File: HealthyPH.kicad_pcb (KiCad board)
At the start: 2 copper layers, 68.4 x 53.2 mm, 33 parts, among them CON1 LB_BarrelJack, P1 CONN_6, P2 V+_WallWart, Q1 TIP122, U1 LMV341, U2 MCP3901, U5 LM7805, X1 CRYSTAL

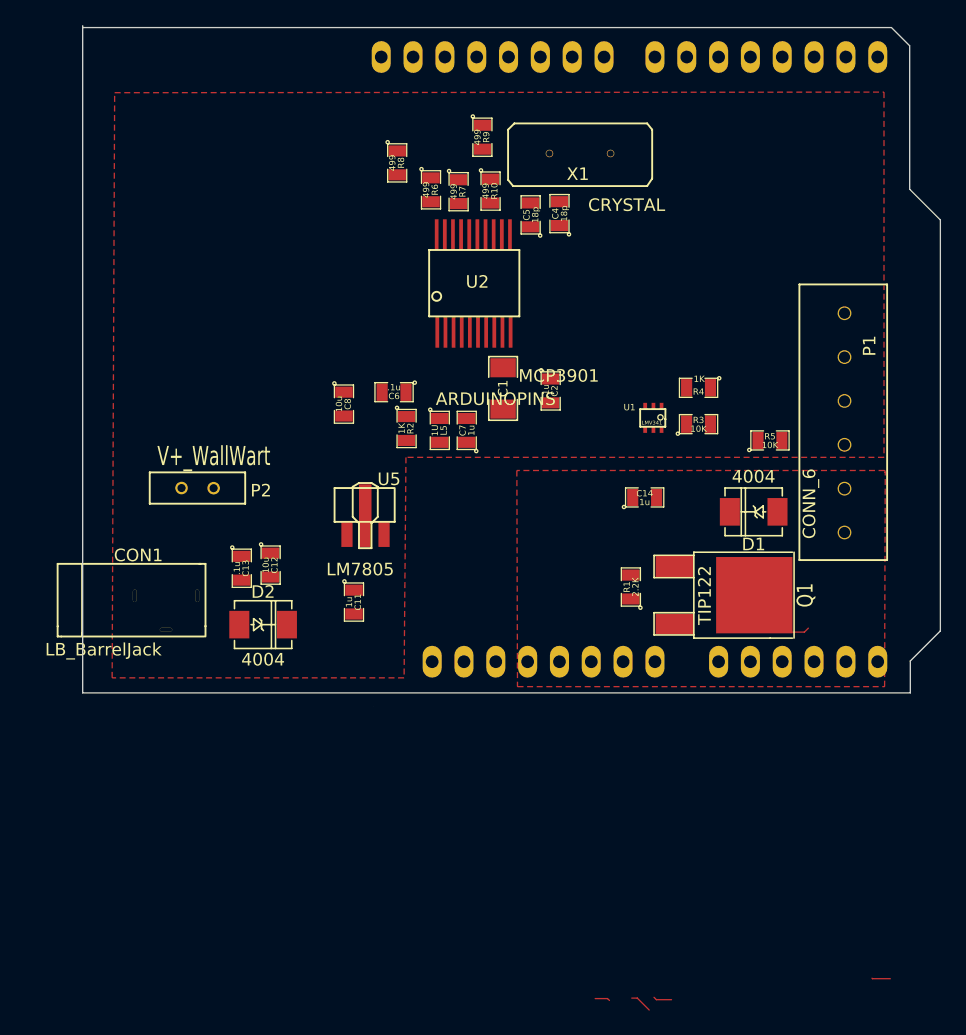
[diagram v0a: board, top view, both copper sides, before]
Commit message: added 2nd pump in circuit to accomodate pH UP
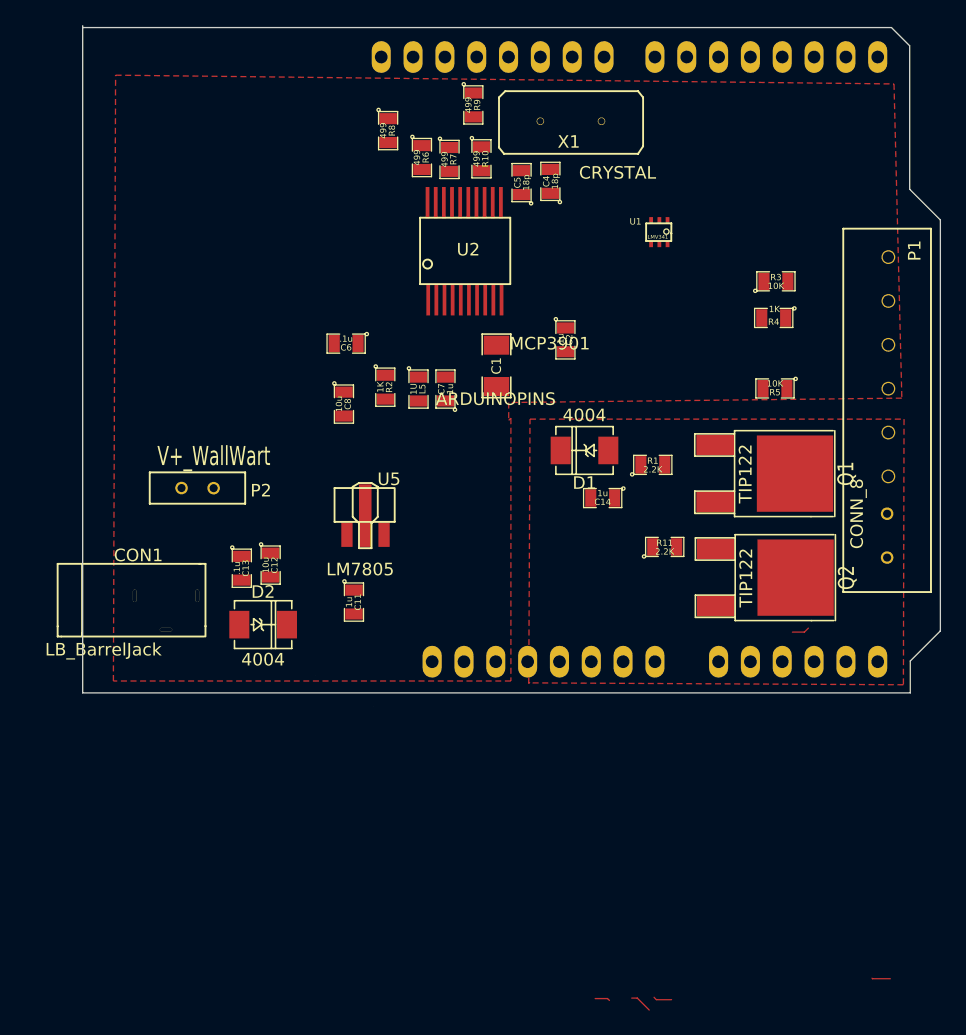
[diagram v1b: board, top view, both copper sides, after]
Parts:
- added Q2: TIP122, DPAK2, F.Cu at (201.6, 109.0)
- added R11: 2.2K, SM0805, F.Cu at (197.4, 106.5)
- P1: value CONN_6 -> CONN_8; footprint LB_6PosTB -> LB_8PosTB
- moved U1 14.8 mm to (198.0, 82.1)
- moved D1 14.4 mm to (191.1, 98.8)
- moved R3 13.0 mm to (206.3, 85.3)
- moved Q1 10.2 mm to (201.5, 100.7)
- moved R1 9.91 mm to (196.5, 100.0), turned to 0 degrees
- moved P1 9.65 mm to (218.7, 81.2)
- moved R4 8.19 mm to (206.2, 88.3)
- moved C6 5.44 mm to (172.0, 90.3)
- moved C2 4.24 mm to (189.5, 90.0)
- moved R5 4.17 mm to (206.2, 93.9), turned to 180 degrees
- moved C7 3.71 mm to (179.9, 94.0)
- moved L5 3.71 mm to (177.8, 94.0)
- moved R2 3.71 mm to (175.2, 93.8)
- moved C14 3.35 mm to (192.5, 102.7), turned to 180 degrees
- moved C4 2.68 mm to (188.3, 77.4)
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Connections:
- net /Arduino/PHPUMPDOWN renamed /Pumps/DownPump
- net /Pumps/Pump_SW renamed /Pumps/SW_DownPump
- ARD1 pad 13: /Arduino/~DR -> (no net)
- ARD1 pad 15: /Arduino/~RESET -> (no net)
- ARD1 pad 21: /Arduino/~CS -> (no net)
- ARD1 pad 22: /Arduino/MOSI -> (no net)
- ARD1 pad 23: /Arduino/MISO -> (no net)
- ARD1 pad 24: /Arduino/SCLK -> (no net)
- ARD1 pad 6: (no net) -> /Arduino/PumpUp
- D1 pad 1: /Pumps/Pump_V+ -> /Pumps/V+_DownPump
- P1 pad 5: /Pumps/Pump_V+ -> /Pumps/V+_DownPump
- R10 pad 1: /Arduino/~DR -> (no net)
- R6 pad 1: /Arduino/SCLK -> (no net)
- R7 pad 1: /Arduino/MISO -> (no net)
- R8 pad 1: /Arduino/MOSI -> (no net)
- R9 pad 1: /Arduino/~CS -> (no net)
- U2 pad 1: /Arduino/~RESET -> (no net)
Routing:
- net /Pumps/SW_DownPump: track 1.40 -> 0.00 mm, vias 1 -> 0
- net (no net): track 5.95 -> 7.35 mm, vias 5 -> 6

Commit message: changed op amp from LMV341 to MCP6241
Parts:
- U1: value LMV341 -> MCP6241; footprint LB_LMV341 -> SOT23-5
- U5: footprint LB_SOT89 -> LB_SOT89_3
- moved U5 1.95 mm to (173.5, 104.0)
- moved U1 1.57 mm to (197.2, 80.8), turned to 90 degrees
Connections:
- U1 pad 1: /pH/pH_V+(in) -> /Digital Access/pH_ADC+
- U1 pad 2: /Digital Access/pH_ADC+ -> AGND
- U1 pad 3: /Digital Access/pH_ADC+ -> /pH/pH_V+(in)
- U1 pad 4: AGND -> /Digital Access/pH_ADC+
- U1 pad 5: (no net) -> /pH/V+_WallWart
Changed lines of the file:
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@@
 (kicad_pcb (version 3) (host pcbnew "(2013-07-07 BZR 4022)-stable")
   (general
-    (links 71)
+    (links 73)
     (no_connects 56)
-    (area 144.518999 64.828999 223.816524 143.513001)
+    (area 150.949999 64.899999 219.500001 118.250001)
     (thickness 1.6)
     (drawings 9)
@@
     (15 F.Cu signal)
     (0 B.Cu signal)
-    (16 B.Adhes user)
+    (16 B.Adhes user hide)
     (17 F.Adhes user)
-    (18 B.Paste user)
-    (19 F.Paste user)
-    (20 B.SilkS user)
+    (18 B.Paste user hide)
+    (19 F.Paste user hide)
+    (20 B.SilkS user hide)
     (21 F.SilkS user)
-    (22 B.Mask user)
-    (23 F.Mask user)
-    (24 Dwgs.User user)
-    (25 Cmts.User user)
+    (22 B.Mask user hide)
+    (23 F.Mask user hide)
+    (24 Dwgs.User user hide)
+    (25 Cmts.User user hide)
     (26 Eco1.User user)
-    (27 Eco2.User user)
+    (27 Eco2.User user hide)
     (28 Edge.Cuts user)
   )
@@
     (visible_elements 7FFFFFFF)
     (pcbplotparams
-      (layerselection 3178497)
-      (usegerberextensions true)
-      (excludeedgelayer true)
+      (layerselection 8388608)
+      (usegerberextensions false)
+      (excludeedgelayer false)
       (linewidth 0.150000)
-      (plotframeref false)
+      (plotframeref true)
       (viasonmask false)
       (mode 1)
@@
       (plotothertext true)
       (plotinvisibletext false)
-      (padsonsilk false)
+      (padsonsilk true)
       (subtractmaskfromsilk false)
-      (outputformat 1)
+      (outputformat 2)
       (mirror false)
-      (drillshape 1)
+      (drillshape 0)
       (scaleselection 1)
       (outputdirectory ""))
@@
     )
   )
-  (module LB_SOT89 (layer F.Cu)
-    (at 172.05 105.35)
-    (fp_text reference U5 (at 3.4 -4.2) (layer F.SilkS)
-      (effects (font (size 1 1) (thickness 0.15)))
-    )
-    (fp_text value LM7805 (at 1.1 3) (layer F.SilkS)
-      (effects (font (size 1 1) (thickness 0.15)))
-    )
-    (fp_line (start 2.5 -3.6) (end 2 -3.9) (layer F.SilkS) (width 0.15))
-    (fp_line (start 2 -3.9) (end 1 -3.9) (layer F.SilkS) (width 0.15))
-    (fp_line (start 1 -3.9) (end 0.5 -3.6) (layer F.SilkS) (width 0.15))
-    (fp_line (start 0.5 -3.6) (end 0.5 -1.2) (layer F.SilkS) (width 0.15))
-    (fp_line (start 2.5 -3.3) (end 2.5 -3.6) (layer F.SilkS) (width 0.15))
-    (fp_line (start 2.5 -1.2) (end 2.5 -3.2) (layer F.SilkS) (width 0.15))
-    (fp_line (start 1 -0.7) (end 0.5 -1.2) (layer F.SilkS) (width 0.15))
-    (fp_line (start 2 -0.7) (end 2.5 -1.2) (layer F.SilkS) (width 0.15))
-    (fp_line (start 1 -0.7) (end 1 1.3) (layer F.SilkS) (width 0.15))
-    (fp_line (start 1 1.3) (end 2 1.3) (layer F.SilkS) (width 0.15))
-    (fp_line (start 2 1.3) (end 2 -0.7) (layer F.SilkS) (width 0.15))
-    (fp_line (start 3.75 -3.5) (end -0.95 -3.5) (layer F.SilkS) (width 0.15))
-    (fp_line (start -0.95 -3.5) (end -0.95 -0.8) (layer F.SilkS) (width 0.15))
-    (fp_line (start -0.95 -0.8) (end 3.85 -0.8) (layer F.SilkS) (width 0.15))
-    (fp_line (start 3.85 -0.8) (end 3.85 -3.5) (layer F.SilkS) (width 0.15))
-    (pad 1 smd rect (at 0.04 0.2) (size 0.9 2)
-      (layers F.Cu F.Paste F.Mask)
-      (net 21 AGND)
-    )
-    (pad 3 smd rect (at 3 0.2) (size 0.9 2)
-      (layers F.Cu F.Paste F.Mask)
-      (net 18 "/Wall Wart/Vin")
-    )
-    (pad 2 smd rect (at 1.5 -1.3) (size 1 5)
-      (layers F.Cu F.Paste F.Mask)
-      (net 1 +5V)
-    )
-  )
   (module LB_BarrelJack (layer F.Cu)
     (at 148.95 107.95)
@@
     )
   )
-  (module LB_LMV341 (layer F.Cu)
-    (at 197.975 82.125 180)
-    (attr smd)
-    (fp_text reference U1 (at 2.86 1.54 180) (layer F.SilkS)
-      (effects (font (size 0.508 0.508) (thickness 0.0762)))
-    )
-    (fp_text value LMV341 (at 1.07 0.31 180) (layer F.SilkS)
-      (effects (font (size 0.3 0.3) (thickness 0.075)))
-    )
-    (fp_circle (center 0.39 0.74) (end 0.58 0.83) (layer F.SilkS) (width 0.1))
-    (fp_line (start 2.01 0) (end 2.01 1.39) (layer F.SilkS) (width 0.15))
-    (fp_line (start -0.01 1.41) (end 0 0.6) (layer F.SilkS) (width 0.15))
-    (fp_line (start 0 0.6) (end -0.01 0.6) (layer F.SilkS) (width 0.15))
-    (fp_line (start 0 -0.00972) (end 2 -0.00972) (layer F.SilkS) (width 0.15))
-    (fp_line (start 2 1.39972) (end 0 1.39972) (layer F.SilkS) (width 0.15))
-    (fp_line (start 0.00084 0.58972) (end 0.00084 -0.00972) (layer F.SilkS) (width 0.15))
-    (pad 6 smd rect (at 0.3 -0.25 180) (size 0.3 0.5)
-      (layers F.Cu F.Paste F.Mask)
-      (net 19 /pH/V+_WallWart)
-    )
-    (pad 5 smd rect (at 0.95 -0.25 180) (size 0.3 0.5)
-      (layers F.Cu F.Paste F.Mask)
-    )
-    (pad 3 smd rect (at 1.61 1.65 180) (size 0.3 0.5)
-      (layers F.Cu F.Paste F.Mask)
-      (net 10 "/Digital Access/pH_ADC+")
-    )
-    (pad 2 smd rect (at 0.95 1.65 180) (size 0.3 0.5)
-      (layers F.Cu F.Paste F.Mask)
-      (net 10 "/Digital Access/pH_ADC+")
-    )
-    (pad 1 smd rect (at 0.3 1.65 180) (size 0.3 0.5)
-      (layers F.Cu F.Paste F.Mask)
-      (net 20 "/pH/pH_V+(in)")
-    )
-    (pad 4 smd rect (at 1.61 -0.25) (size 0.3 0.5)
-      (layers F.Cu F.Paste F.Mask)
-      (net 21 AGND)
-    )
-    (model smd\SOT23_6.wrl
-      (at (xyz 0 0 0))
-      (scale (xyz 0.06 0.06 0.06))
-      (rotate (xyz 0 0 -180))
-    )
-  )
   (module LB_2TB (layer F.Cu)
     (at 156.35 103.1)
@@
     )
   )
+  (module LB_SOT89_3 (layer F.Cu)
+    (at 173.5 104.05)
+    (descr "SOT89-3, Housing,")
+    (tags "SOT89-3, Housing,")
+    (attr smd)
+    (fp_text reference U5 (at -0.09906 -4.24942) (layer F.SilkS)
+      (effects (font (size 1.524 1.524) (thickness 0.3048)))
+    )
+    (fp_text value LM7805 (at -0.20066 4.59994) (layer F.SilkS) hide
+      (effects (font (size 1.524 1.524) (thickness 0.3048)))
+    )
+    (fp_line (start -1.89992 0.20066) (end -1.651 -0.09906) (layer F.SilkS) (width 0.381))
+    (fp_line (start -1.651 -0.09906) (end -1.5494 -0.24892) (layer F.SilkS) (width 0.381))
+    (fp_line (start -1.5494 -0.24892) (end -1.5494 0.59944) (layer F.SilkS) (width 0.381))
+    (fp_line (start -2.25044 -1.30048) (end -2.25044 0.50038) (layer F.SilkS) (width 0.381))
+    (fp_line (start -2.25044 -1.30048) (end -1.6002 -1.30048) (layer F.SilkS) (width 0.381))
+    (fp_line (start 2.25044 -1.30048) (end 2.25044 0.50038) (layer F.SilkS) (width 0.381))
+    (fp_line (start 2.25044 -1.30048) (end 1.6002 -1.30048) (layer F.SilkS) (width 0.381))
+    (pad 1 smd rect (at -1.50114 1.85166) (size 1.00076 1.50114)
+      (layers F.Cu F.Paste F.Mask)
+      (net 21 AGND)
+    )
+    (pad 2 smd rect (at 0 1.85166) (size 1.00076 1.50114)
+      (layers F.Cu F.Paste F.Mask)
+      (net 1 +5V)
+    )
+    (pad 3 smd rect (at 1.50114 1.85166) (size 1.00076 1.50114)
+      (layers F.Cu F.Paste F.Mask)
+      (net 18 "/Wall Wart/Vin")
+    )
+    (pad 2 smd rect (at 0 -1.09982) (size 1.99898 2.99974)
+      (layers F.Cu F.Paste F.Mask)
+      (net 1 +5V)
+    )
+    (pad 2 smd trapezoid (at 0 0.7493 180) (size 1.50114 0.7493) (rect_delta 0 0.50038 )
+      (layers F.Cu F.Paste F.Mask)
+      (net 1 +5V)
+    )
+    (model SOT89-3_SOT89-5_Housing_Wings3d_RevA_02Sep2012/SOT89-3_Housing_Faktor03937_RevA_02Sep2012.wrl
+      (at (xyz 0 0 0))
+      (scale (xyz 0.3937 0.3937 0.3937))
+      (rotate (xyz 0 0 0))
+    )
+  )
+  (module SOT23-5 (layer F.Cu)
+    (at 197.175 80.775 90)
+    (attr smd)
+    (fp_text reference U1 (at 2.19964 -0.29972 180) (layer F.SilkS)
+      (effects (font (size 0.635 0.635) (thickness 0.127)))
+    )
+    (fp_text value MCP6241 (at 0 0 90) (layer F.SilkS)
+      (effects (font (size 0.635 0.635) (thickness 0.127)))
+    )
+    (fp_line (start 1.524 -0.889) (end 1.524 0.889) (layer F.SilkS) (width 0.127))
+    (fp_line (start 1.524 0.889) (end -1.524 0.889) (layer F.SilkS) (width 0.127))
+    (fp_line (start -1.524 0.889) (end -1.524 -0.889) (layer F.SilkS) (width 0.127))
+    (fp_line (start -1.524 -0.889) (end 1.524 -0.889) (layer F.SilkS) (width 0.127))
+    (pad 1 smd rect (at -0.9525 1.27 90) (size 0.508 0.762)
+      (layers F.Cu F.Paste F.Mask)
+      (net 10 "/Digital Access/pH_ADC+")
+    )
+    (pad 3 smd rect (at 0.9525 1.27 90) (size 0.508 0.762)
+      (layers F.Cu F.Paste F.Mask)
+      (net 20 "/pH/pH_V+(in)")
+    )
+    (pad 5 smd rect (at -0.9525 -1.27 90) (size 0.508 0.762)
+      (layers F.Cu F.Paste F.Mask)
+      (net 19 /pH/V+_WallWart)
+    )
+    (pad 2 smd rect (at 0 1.27 90) (size 0.508 0.762)
+      (layers F.Cu F.Paste F.Mask)
+      (net 21 AGND)
+    )
+    (pad 4 smd rect (at 0.9525 -1.27 90) (size 0.508 0.762)
+      (layers F.Cu F.Paste F.Mask)
+      (net 10 "/Digital Access/pH_ADC+")
+    )
+    (model smd/SOT23_5.wrl
+      (at (xyz 0 0 0))
+      (scale (xyz 0.1 0.1 0.1))
+      (rotate (xyz 0 0 0))
+    )
+  )
